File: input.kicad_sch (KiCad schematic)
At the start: 35 parts, among them U5 74HC165, U6 74HC165, U8 Sparkfun_Pro_Micro

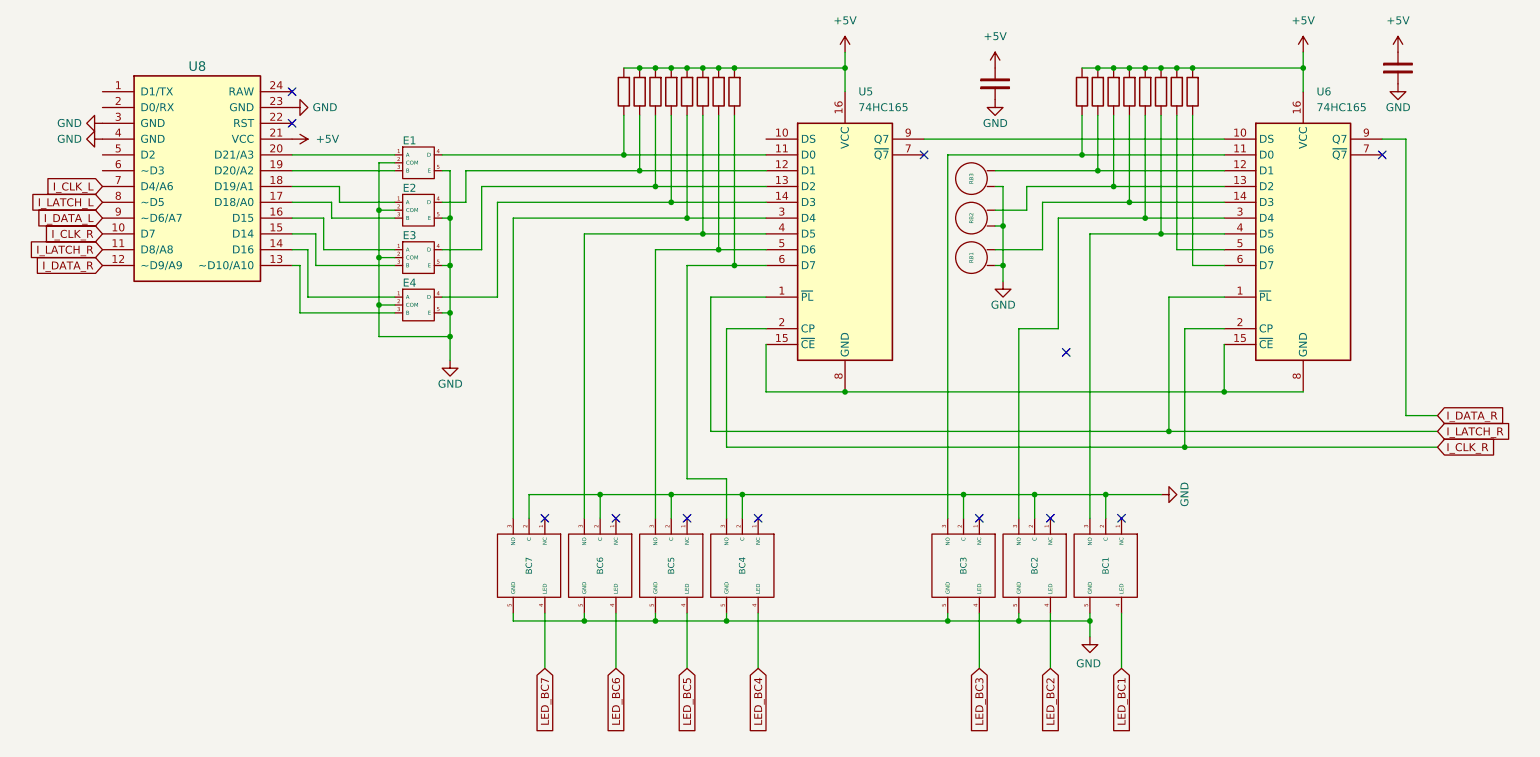
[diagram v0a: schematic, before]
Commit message: New schematic
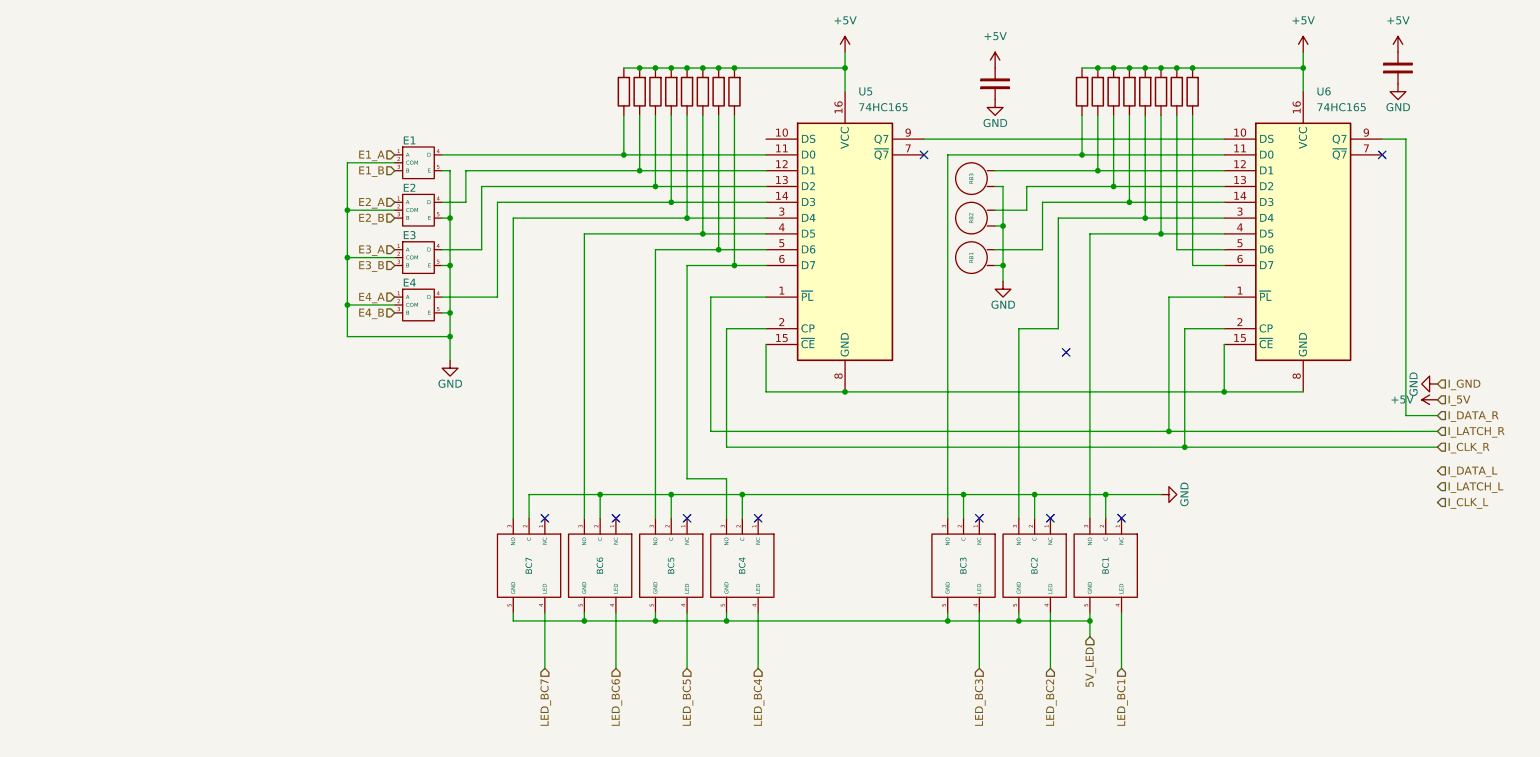
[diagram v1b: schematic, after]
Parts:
- removed U8: Sparkfun_Pro_Micro, Arduino:Sparkfun_Pro_Micro, symbol Arduino:Sparkfun_Pro_Micro
- BC1, BC2, BC3, BC4, BC5, BC6, BC7, E1, E2, E3, E4, RB1, RB2, RB3: value ~ -> (none)
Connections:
- net GND: no longer BC1.5 (GND), BC2.5 (GND), BC3.5 (GND), BC4.5 (GND), BC5.5 (GND), BC6.5 (GND), BC7.5 (GND)
- net E3_A: now reaches E3.1 (A)
- net E3_B: now reaches E3.3 (B)
- net E4_B: now reaches E4.3 (B)
- net E4_A: now reaches E4.1 (A)
- net E2_B: now reaches E2.3 (B)
- net E2_A: now reaches E2.1 (A)
- net E1_B: now reaches E1.3 (B)
- net E1_A: now reaches E1.1 (A)
- new net 5V_LED: BC1.5 (GND), BC2.5 (GND), BC3.5 (GND), BC4.5 (GND), BC5.5 (GND), BC6.5 (GND), BC7.5 (GND)
- no-connect marks 12 -> 10

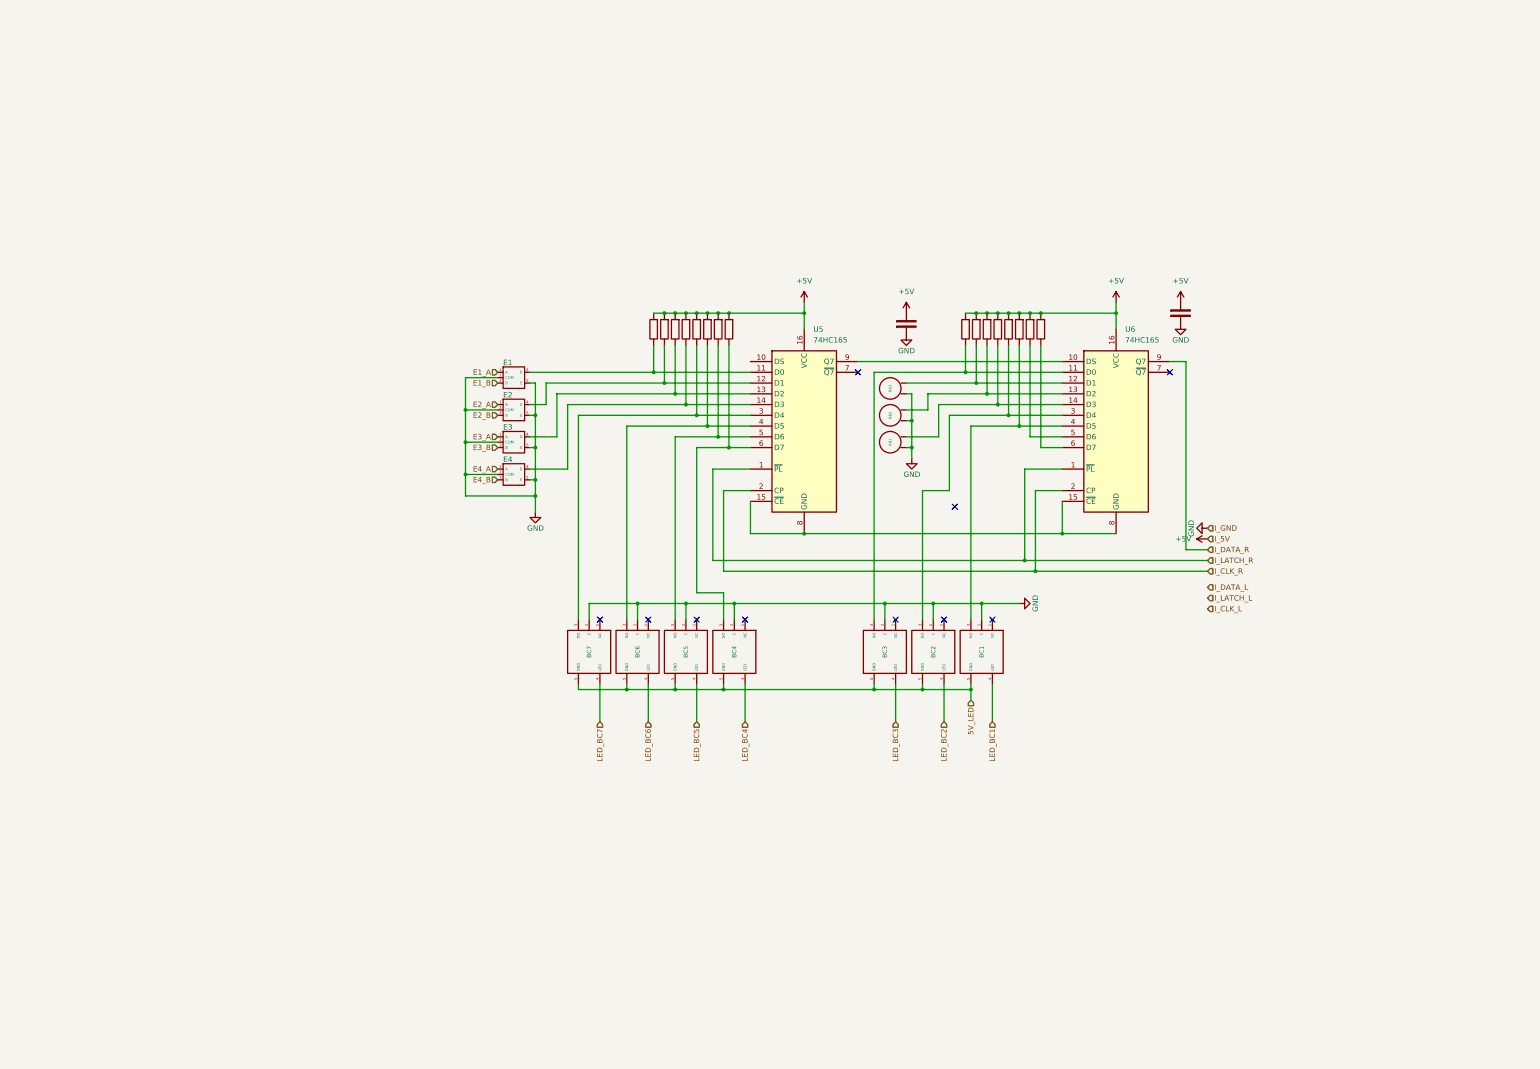
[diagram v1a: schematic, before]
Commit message: Update schematic with nearly everything
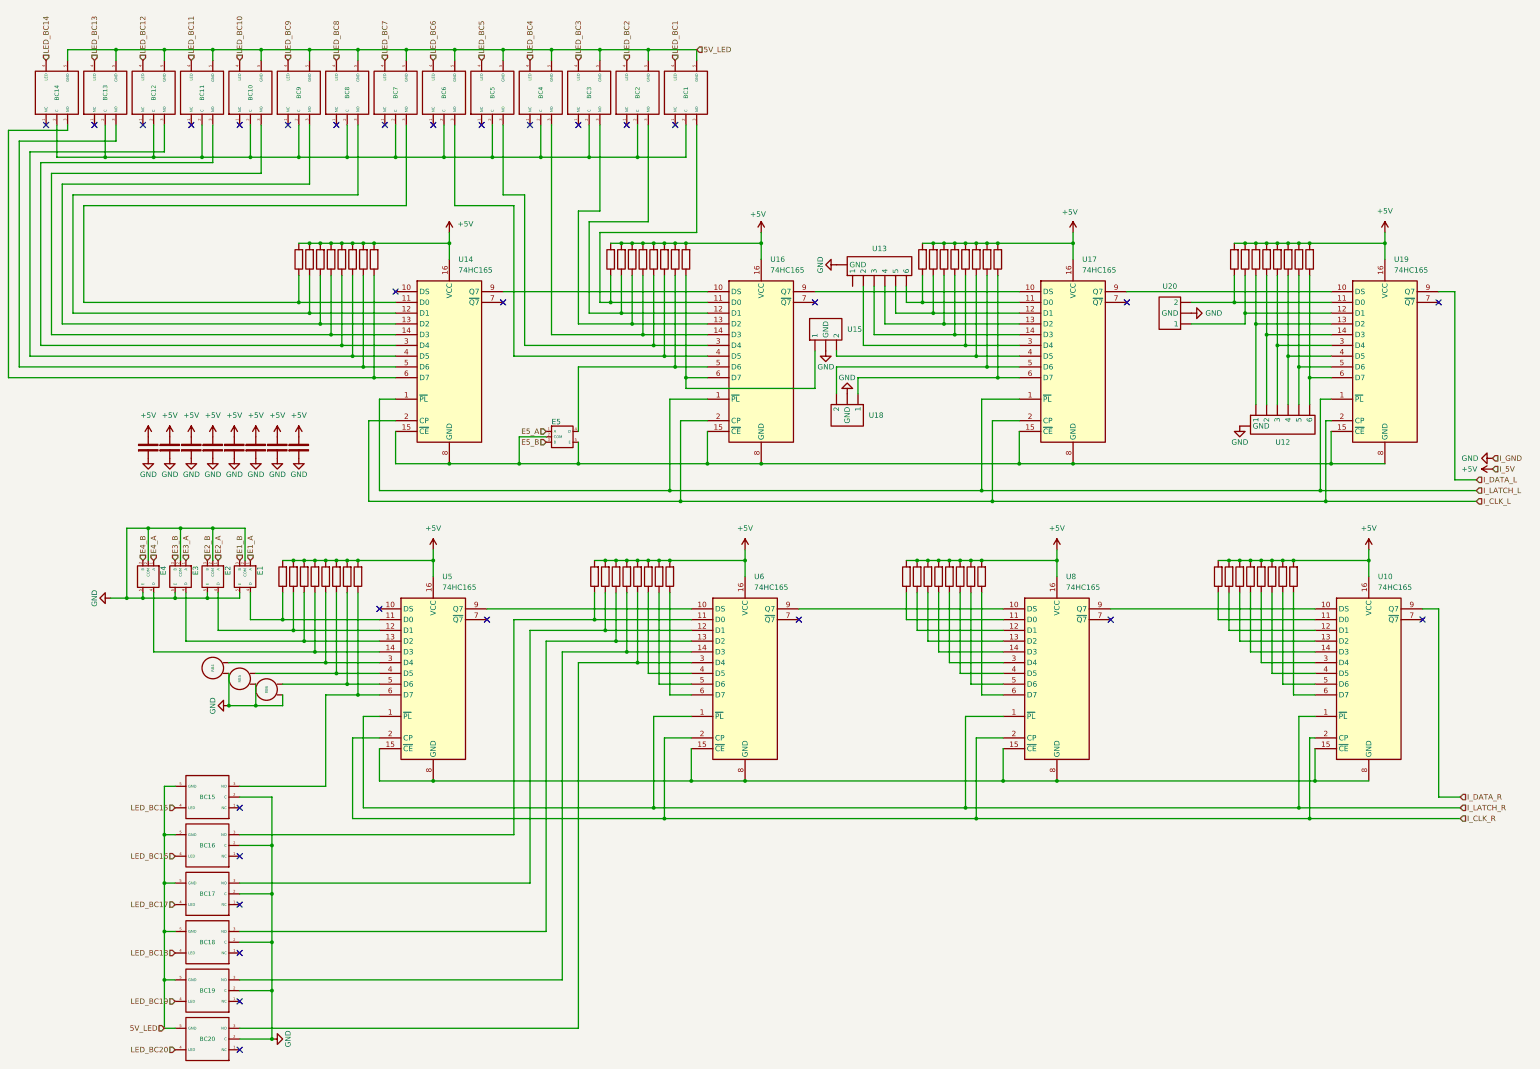
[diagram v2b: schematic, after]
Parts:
- removed RB1, RB2, RB3: (no value), mf:r_but, symbol _mf:r_but
- added BC1, BC11, BC12, BC13, BC14, BC15, BC16, BC17, BC2, BC3, BC4, BC5, BC6: (no value), mf:sq_but, symbol _mf:sq_but
- added C10, C11, C5, C7, C8, C9: Capacitor_NP, Capacitor_THT:C_Disc_D3.0mm_W2.0mm_P2.50mm, symbol PCM_SL_Devices:Capacitor_NP
- added E5: (no value), mf:ec11-ext, symbol _mf:ec11-ext
- added R34, R35, R36, R38, R39, R40, R41, R42, R43, R44, R45, R46, R47, R48, R49, R50, R51, R52, R53, R54, R55, R56, R57, R58, R59, R60, R61, R62, R63, R64, R65, R66, R67, R68, R69, R70, R71, R72, R73, R74, R75, R76, R77, R78, R79, R80, R81, R82: Resistor, Resistor_THT:R_Axial_DIN0207_L6.3mm_D2.5mm_P10.16mm_Horizontal, symbol PCM_SL_Devices:Resistor
- added RB4, RB5, RB6: (no value), mf:r_but, symbol _mf:r_but
- added U10, U14, U16, U17, U19, U8: 74HC165, Package_DIP:DIP-16_W7.62mm_LongPads, symbol 74xx:74HC165
- added U12, U13: (no value), symbol _mf:5/6_pos_switch_
- added U15, U18, U20: (no value), symbol _mf:3_pos_switch
- renumbered BC4 to BC10, BC7 to BC18, BC6 to BC19, BC5 to BC20, BC3 to BC7, BC2 to BC8, BC1 to BC9
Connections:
- net +5V: now also C10.2, C11.2, C5.2, C7.2, C8.2, C9.2, R34.1, R35.1, R36.1, R38.1, R39.1, R40.1, R41.1, R42.1, R43.1, R44.1, R45.1, R46.1, R47.1, R48.1, R49.1, R50.1, R51.1, R52.1, R53.1, R54.1, R55.1, R56.1, R57.1, R58.1, R59.1, R60.1, R61.1, R62.1, R63.1, R64.1, R65.1, R66.1, R67.1, R68.1, R69.1, R70.1, R71.1, R72.1, R73.1, R74.1, R75.1, R76.1, R77.1, R78.1, R79.1, R80.1, R81.1, R82.1, U10.16 (VCC), U14.16 (VCC), U16.16 (VCC), U17.16 (VCC), U19.16 (VCC), U8.16 (VCC)
- net 5V_LED: now also BC1.5 (GND), BC11.5 (GND), BC12.5 (GND), BC13.5 (GND), BC14.5 (GND), BC15.5 (GND), BC16.5 (GND), BC17.5 (GND), BC2.5 (GND), BC3.5 (GND), BC4.5 (GND), BC5.5 (GND), BC6.5 (GND)
- net GND: now also BC15.2 (C), BC16.2 (C), BC17.2 (C), C10.1, C11.1, C5.1, C7.1, C8.1, C9.1, RB4.1, RB5.1, RB6.1, U12. (GND), U13. (GND), U15. (2), U18. (2), U20. (2); no longer BC10.2 (C), BC7.2 (C), BC8.2 (C), BC9.2 (C)
- net I_CLK_L: now also U14.2 (CP), U16.2 (CP), U17.2 (CP), U19.2 (CP)
- net I_CLK_R: now also U10.2 (CP), U8.2 (CP)
- net I_DATA_L: now also U19.9 (Q7)
- net I_DATA_R: now also U10.9 (Q7); no longer U6.9 (Q7)
- net I_LATCH_L: now also U14.1 (~{PL}), U16.1 (~{PL}), U17.1 (~{PL}), U19.1 (~{PL})
- net I_LATCH_R: now also U10.1 (~{PL}), U8.1 (~{PL})
- net LED_BC1: now also BC1.4 (LED); no longer BC9.4 (LED)
- net LED_BC2: now also BC2.4 (LED); no longer BC8.4 (LED)
- net LED_BC3: now also BC3.4 (LED); no longer BC7.4 (LED)
- net LED_BC4: now also BC4.4 (LED); no longer BC10.4 (LED)
- net LED_BC5: now also BC5.4 (LED); no longer BC20.4 (LED)
- net LED_BC6: now also BC6.4 (LED); no longer BC19.4 (LED)
- net LED_BC7: now also BC7.4 (LED); no longer BC18.4 (LED)
- net at R21.2, U5.3 (D4): now also RB4.2; no longer BC18.3 (NO)
- net at R25.2, U6.11 (D0): now also BC16.3 (NO); no longer BC7.3 (NO)
- net at R26.2, U6.12 (D1): now also BC17.3 (NO)
- net at R27.2, U6.13 (D2): now also BC18.3 (NO)
- net at R28.2, U6.14 (D3): now also BC19.3 (NO)
- net at U5.15 (~{CE}), U5.8 (GND), U6.15 (~{CE})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: now also U10.15 (~{CE}), U10.8 (GND), U8.15 (~{CE}), U8.8 (GND)
- net at R29.2, U6.3 (D4): now also BC20.3 (NO); no longer BC8.3 (NO)
- net at R30.2, U6.4 (D5): no longer BC9.3 (NO)
- net at R22.2, U5.4 (D5): now also RB5.2; no longer BC19.3 (NO)
- net at R24.2, U5.6 (D7): now also BC15.3 (NO); no longer BC10.3 (NO)
- net at R23.2, U5.5 (D6): now also RB6.2; no longer BC20.3 (NO)
- new net: BC11.3 (NO), R55.2, U14.3 (D4)
- new net: U6.9 (Q7), U8.10 (DS)
- new net: R42.2, U8.6 (D7)
- new net: R48.2, U10.4 (D5)
- new net: R79.2, U12. (GND), U19.3 (D4)
- new net: U14.9 (Q7), U16.10 (DS)
- new net: BC1.3 (NO), R59.2, U16.11 (D0)
- new net: BC2.3 (NO), R60.2, U16.12 (D1)
- new net: BC3.3 (NO), R61.2, U16.13 (D2)
- new net: BC4.3 (NO), R62.2, U16.14 (D3)
- new net: E5.2 (COM), E5.5 (E), U14.15 (~{CE}), U14.8 (GND), U16.15 (~{CE}), U16.8 (GND), U17.15 (~{CE}), U17.8 (GND), U19.15 (~{CE}), U19.8 (GND)
- new net: BC5.3 (NO), R63.2, U16.3 (D4)
- new net: BC6.3 (NO), R64.2, U16.4 (D5)
- new net: E5.4 (D), R65.2, U16.5 (D6)
- new net: R66.2, U15. (2), U16.6 (D7)
- new net: U16.9 (Q7), U17.10 (DS)
- new net: BC1.2 (C), BC10.2 (C), BC11.2 (C), BC12.2 (C), BC13.2 (C), BC14.2 (C), BC2.2 (C), BC3.2 (C), BC4.2 (C), BC5.2 (C), BC6.2 (C), BC7.2 (C), BC8.2 (C), BC9.2 (C)
- new net: BC7.3 (NO), R51.2, U14.11 (D0)
- new net: BC12.3 (NO), R56.2, U14.4 (D5)
- new net: R76.2, U19.12 (D1), U20. (2)
- new net: R81.2, U12. (GND), U19.5 (D6)
- new net: R38.2, U8.14 (D3)
- new net: R77.2, U12. (GND), U19.13 (D2)
- new net: R78.2, U12. (GND), U19.14 (D3)
- new net: R80.2, U12. (GND), U19.4 (D5)
- new net: R82.2, U12. (GND), U19.6 (D7)
- new net: BC13.3 (NO), R57.2, U14.5 (D6)
- new net: BC9.3 (NO), R53.2, U14.13 (D2)
- new net: R49.2, U10.5 (D6)
- new net: BC14.3 (NO), R58.2, U14.6 (D7)
- new net: R39.2, U8.3 (D4)
- new net: R72.2, U15. (2), U17.4 (D5)
- new net: R50.2, U10.6 (D7)
- new net: R73.2, U17.5 (D6), U18. (2)
- new net: R41.2, U8.5 (D6)
- new net: R67.2, U13. (GND), U17.11 (D0)
- new net: R68.2, U13. (GND), U17.12 (D1)
- new net: R69.2, U13. (GND), U17.13 (D2)
- new net: R70.2, U13. (GND), U17.14 (D3)
- new net: R71.2, U13. (GND), U17.3 (D4)
- new net: R74.2, U17.6 (D7), U18. (2)
- new net: U17.9 (Q7), U19.10 (DS)
- new net: R45.2, U10.13 (D2)
- new net: R75.2, U19.11 (D0), U20. (2)
- new net: BC10.3 (NO), R54.2, U14.14 (D3)
- new net: BC8.3 (NO), R52.2, U14.12 (D1)
- new net: R34.2, U8.11 (D0)
- new net: R44.2, U10.12 (D1)
- new net: R36.2, U8.13 (D2)
- new net: U10.10 (DS), U8.9 (Q7)
- new net: R43.2, U10.11 (D0)
- new net: R46.2, U10.14 (D3)
- new net: R47.2, U10.3 (D4)
- new net: R35.2, U8.12 (D1)
- new net: R40.2, U8.4 (D5)
- new net E5_A: E5.1 (A)
- new net E5_B: E5.3 (B)
- new net LED_BC10: BC10.4 (LED)
- new net LED_BC11: BC11.4 (LED)
- new net LED_BC12: BC12.4 (LED)
- new net LED_BC13: BC13.4 (LED)
- new net LED_BC14: BC14.4 (LED)
- new net LED_BC15: BC15.4 (LED)
- new net LED_BC16: BC16.4 (LED)
- new net LED_BC17: BC17.4 (LED)
- new net LED_BC18: BC18.4 (LED)
- new net LED_BC19: BC19.4 (LED)
- new net LED_BC20: BC20.4 (LED)
- new net LED_BC8: BC8.4 (LED)
- new net LED_BC9: BC9.4 (LED)
- no-connect marks 10 -> 30
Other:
- moved on the sheet: BC10, BC18, BC19, BC20, BC7, BC8, BC9, E1, E2, E3, E4, U5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

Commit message: New pcb and 3 pos switch footprint
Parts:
- U15, U18, U20: footprint (none) -> mf:3posswitch
- renumbered C5 to C1, C7 to C2, C11 to C3, C10 to C4, C9 to C5, C8 to C6, C2 to C7, C3 to C8
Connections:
- net GND: now also U15.3 (GND), U18.3 (GND), U20.3 (GND); no longer U15. (2), U18. (2), U20. (2)
- net at R66.2, U16.6 (D7): now also U15.1; no longer U15. (2)
- net at R76.2, U19.12 (D1): now also U20.1; no longer U20. (2)
- net at R72.2, U17.4 (D5): now also U15.2; no longer U15. (2)
- net at R73.2, U17.5 (D6): now also U18.2; no longer U18. (2)
- net at R74.2, U17.6 (D7): now also U18.1; no longer U18. (2)
- net at R75.2, U19.11 (D0): now also U20.2; no longer U20. (2)
